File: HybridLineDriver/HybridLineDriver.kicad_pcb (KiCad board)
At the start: 2 copper layers, 100 x 50 mm, 60 parts, among them J1 XLR3, J2 Conn_01x03, J3 Conn_01x02, J4 XLR3, J5 Conn_01x02, U1 OPA1679, U2 OPA1679

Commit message: added comments
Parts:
- moved C14 9.23 mm to (114.3, 91.4)
- moved R24 5.43 mm to (109.2, 92.7), turned to -90 degrees
- moved C18 5.09 mm to (91.4, 91.4)
- moved J1 4.84 mm to (81.9, 85.7), turned to 90 degrees
- moved J4 4.26 mm to (101.0, 85.7), turned to 90 degrees
- moved R29 3.49 mm to (96.5, 93.2), turned to 90 degrees
- moved J3 2.62 mm to (80.0, 124.5), turned to -90 degrees
- moved R18 2.62 mm to (76.8, 88.9)
- moved J5 2.62 mm to (93.3, 124.5), turned to -90 degrees
- moved C6 2.29 mm to (72.4, 94.0)
- moved C2 1.77 mm to (80.0, 100.3)
- moved C5 1.42 mm to (72.4, 120.0)
- moved R6 1.34 mm to (83.0, 95.2)
- moved RV2 1.27 mm to (112.4, 123.9)
- moved R26 1.08 mm to (107.3, 123.9)
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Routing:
- net Net-(C18-Pad1): track 6.72 -> 17.7 mm
- net Net-(C14-Pad1): track 6.46 -> 16.6 mm
- net Net-(C6-Pad2): track 16.4 -> 26.1 mm
- net Net-(U2C-+): track 27.1 -> 30.4 mm
- net Net-(J5-Pin_1): track 14.1 -> 11.6 mm
- net Net-(J3-Pin_1): track 7.29 -> 9.46 mm
- net GND: track 32.0 -> 33.2 mm
- net Net-(C5-Pad2): track 19.2 -> 20.3 mm
- net Net-(U2D-+): track 26.0 -> 24.9 mm
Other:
- board text added: "GND"
- board text added: "IN"
- board text added: "IN+"
- board text added: "IN-"
- board text added: "OUT"
- board text added: "OUT+"
- board text added: "OUT-"
- board text added: "V+"
- board text added: "V-"

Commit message: updated comment layout
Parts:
- moved C5 0.64 mm to (71.8, 120.0)
- moved J1 0.64 mm to (81.3, 85.7)
- moved J5 0.64 mm to (94.0, 124.5)
- moved J3 0.63 mm to (80.6, 124.5)
- moved R6 0.44 mm to (82.5, 95.2)
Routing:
- net Net-(J3-Pin_1): track 9.46 -> 10.7 mm
- net Net-(J5-Pin_1): track 11.6 -> 10.8 mm
- net Net-(C6-Pad2): track 26.1 -> 25.4 mm
- net Net-(C5-Pad2): track 20.3 -> 19.7 mm
- net GND: track 33.2 -> 33.7 mm
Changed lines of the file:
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@@
 	(footprint "Connector_PinHeader_2.54mm:PinHeader_1x02_P2.54mm_Vertical"
 		(layer "F.Cu")
-		(at 80.01 124.46 -90)
+		(at 80.645 124.46 -90)
 		(descr "Through hole straight pin header, 1x02, 2.54mm pitch, single row")
 		(tags "Through hole pin header THT 1x02 2.54mm single row")
 		(property "Reference" "J3"
-			(at 0 -2.54 0)
+			(at 0 5.08 0)
 			(unlocked yes)
 			(layer "F.SilkS")
@@
 	(footprint "Resistor_SMD:R_1206_3216Metric"
 		(layer "F.Cu")
-		(at 82.9925 95.25)
+		(at 82.55 95.25)
 		(descr "Resistor SMD 1206 (3216 Metric), square (rectangular) end terminal, IPC_7351 nominal, (Body size source: IPC-SM-782 page 72, https://www.pcb-3d.com/wordpress/wp-content/uploads/ipc-sm-782a_amendment_1_and_2.pdf), generated with kicad-footprint-generator")
 		(tags "resistor")
@@
 		)
 		(property "Value" "100k"
-			(at 0 1.82 360)
+			(at 0 1.82 0)
 			(layer "F.Fab")
 			(effects
@@
 		)
 		(fp_text user "${REFERENCE}"
-			(at 0 0 360)
+			(at 0 0 0)
 			(layer "F.Fab")
 			(effects
@@
 		)
 		(property "Value" "10M"
-			(at 0 1.82 270)
+			(at 0 1.82 -90)
 			(layer "F.Fab")
 			(effects
@@
 		)
 		(fp_text user "${REFERENCE}"
-			(at 0 0 270)
+			(at 0 0 -90)
 			(layer "F.Fab")
 			(effects
@@
 	(footprint "Connector_PinHeader_2.54mm:PinHeader_1x03_P2.54mm_Vertical"
 		(layer "F.Cu")
-		(at 81.915 85.725 90)
+		(at 81.28 85.725 90)
 		(descr "Through hole straight pin header, 1x03, 2.54mm pitch, single row")
 		(tags "Through hole pin header THT 1x03 2.54mm single row")
 		(property "Reference" "J1"
-			(at 0 7.62 0)
+			(at 0 -2.54 0)
 			(unlocked yes)
 			(layer "F.SilkS")
@@
 		)
 		(property "Value" "XLR3"
-			(at 0 7.41 270)
+			(at 0 7.41 -90)
 			(layer "F.Fab")
 			(effects
@@
 		)
 		(fp_text user "${REFERENCE}"
-			(at 0 2.54 360)
+			(at 0 2.54 0)
 			(layer "F.Fab")
 			(effects
@@
 		(tags "Through hole pin header THT 1x03 2.54mm single row")
 		(property "Reference" "J4"
-			(at 0 7.62 0)
+			(at 0 -2.54 0)
 			(unlocked yes)
 			(layer "F.SilkS")
@@
 		)
 		(property "Value" "XLR3"
-			(at 0 7.41 270)
+			(at 0 7.41 -90)
 			(layer "F.Fab")
 			(effects
@@
 		)
 		(fp_text user "${REFERENCE}"
-			(at 0 2.54 360)
+			(at 0 2.54 0)
 			(layer "F.Fab")
 			(effects
@@
 	(footprint "Connector_PinHeader_2.54mm:PinHeader_1x02_P2.54mm_Vertical"
 		(layer "F.Cu")
-		(at 93.345 124.46 -90)
+		(at 93.98 124.46 -90)
 		(descr "Through hole straight pin header, 1x02, 2.54mm pitch, single row")
 		(tags "Through hole pin header THT 1x02 2.54mm single row")
 		(property "Reference" "J5"
-			(at 0 -2.54 0)
+			(at 0 5.08 0)
 			(unlocked yes)
 			(layer "F.SilkS")
@@
 		(tags "Through hole pin header THT 1x03 2.54mm single row")
 		(property "Reference" "J2"
-			(at -2.54 2.54 0)
+			(at 2.54 5.142 0)
 			(unlocked yes)
 			(layer "F.SilkS")
@@
 		(tags "resistor")
 		(property "Reference" "R27"
-			(at 0 -1.82 0)
+			(at 4.445 -0.062 0)
 			(unlocked yes)
 			(layer "F.SilkS")
@@
 	(footprint "Capacitor_THT:CP_Radial_D6.3mm_P2.50mm"
 		(layer "F.Cu")
-		(at 72.39 120.015 -90)
+		(at 71.755 120.015 -90)
 		(descr "CP, Radial series, Radial, pin pitch=2.50mm, , diameter=6.3mm, Electrolytic Capacitor")
 		(tags "CP Radial series Radial pin pitch 2.50mm  diameter 6.3mm Electrolytic Capacitor")
@@
 	)
 	(gr_text "IN"
-		(at 80.645 130.175 90)
+		(at 81.28 130.175 90)
 		(layer "Cmts.User")
 		(effects
@@
 	)
 	(gr_text "OUT"
-		(at 93.98 130.175 90)
+		(at 94.615 130.175 90)
 		(layer "Cmts.User")
 		(effects
@@
 	)
 	(gr_text "GND"
-		(at 82.55 92.71 90)
+		(at 81.915 92.71 90)
 		(layer "Cmts.User")
 		(effects
@@
 	)
 	(gr_text "OUT+"
-		(at 87.63 92.71 90)
+		(at 86.995 92.71 90)
 		(layer "Cmts.User")
 		(effects
@@
 	)
 	(gr_text "GND"
-		(at 91.44 130.175 90)
+		(at 92.075 130.175 90)
 		(layer "Cmts.User")
 		(effects
@@
 	)
 	(gr_text "OUT-"
-		(at 85.09 92.71 90)
+		(at 84.455 92.71 90)
 		(layer "Cmts.User")
 		(effects
@@
 	)
 	(gr_text "GND"
-		(at 78.105 130.175 90)
+		(at 78.74 130.175 90)
 		(layer "Cmts.User")
 		(effects
@@
 	)
 	(segment
+		(start 83.82 85.725)
+		(end 83.82 95.0575)
+		(width 0.254)
+		(layer "F.Cu")
+		(net 4)
+	)
+	(segment
 		(start 80.01 103.83)
 		(end 80.32 103.83)
@@
 	)
 	(segment
-		(start 84.455 85.725)
-		(end 84.455 95.25)
+		(start 84.0125 99.8275)
+		(end 84.0125 95.25)
 		(width 0.254)
 		(layer "F.Cu")
@@
 	)
 	(segment
-		(start 84.455 99.385)
-		(end 84.455 95.25)
+		(start 80.01 103.83)
+		(end 84.0125 99.8275)
 		(width 0.254)
 		(layer "F.Cu")
@@
 	)
 	(segment
-		(start 80.01 103.83)
-		(end 84.455 99.385)
+		(start 83.82 95.0575)
+		(end 84.0125 95.25)
 		(width 0.254)
 		(layer "F.Cu")
@@
 	)
 	(segment
-		(start 52.959 124.6525)
-		(end 53.1515 124.46)
+		(start 69.81 124.46)
+		(end 71.755 122.515)
 		(width 0.25)
 		(layer "F.Cu")
@@
 	)
 	(segment
-		(start 70.445 124.46)
-		(end 72.39 122.515)
+		(start 53.1515 124.46)
+		(end 69.81 124.46)
 		(width 0.25)
 		(layer "F.Cu")
@@
 	)
 	(segment
-		(start 53.1515 124.46)
-		(end 70.445 124.46)
+		(start 52.959 124.6525)
+		(end 53.1515 124.46)
 		(width 0.25)
 		(layer "F.Cu")
@@
 	(segment
 		(start 75.565 120.015)
-		(end 72.39 120.015)
+		(end 71.755 120.015)
+		(width 0.254)
+		(layer "F.Cu")
+		(net 10)
+	)
+	(segment
+		(start 80.645 124.46)
+		(end 80.01 124.46)
 		(width 0.254)
 		(layer "F.Cu")
@@
 	)
 	(segment
-		(start 77.47 83.82)
-		(end 85.09 83.82)
+		(start 72.39 97.48)
+		(end 72.39 97.155)
 		(width 0.254)
 		(layer "F.Cu")
@@
 	)
 	(segment
-		(start 85.09 83.82)
-		(end 86.995 85.725)
+		(start 75.3725 88.9)
+		(end 75.3725 85.9175)
 		(width 0.254)
 		(layer "F.Cu")
@@
 	)
 	(segment
-		(start 72.39 97.48)
-		(end 72.39 97.155)
+		(start 84.455 83.82)
+		(end 86.36 85.725)
 		(width 0.254)
 		(layer "F.Cu")
@@
 	)
 	(segment
-		(start 75.3725 85.9175)
-		(end 77.47 83.82)
+		(start 75.3725 94.1725)
+		(end 75.3725 88.9)
 		(width 0.254)
 		(layer "F.Cu")
@@
 	)
 	(segment
-		(start 75.3725 94.1725)
-		(end 75.3725 88.9)
+		(start 77.47 83.82)
+		(end 84.455 83.82)
 		(width 0.254)
 		(layer "F.Cu")
@@
 	)
 	(segment
-		(start 75.3725 88.9)
-		(end 75.3725 85.9175)
+		(start 75.3725 85.9175)
+		(end 77.47 83.82)
 		(width 0.254)
 		(layer "F.Cu")
@@
 	)
 	(segment
-		(start 79.375 90.805)
-		(end 78.2975 89.7275)
-		(width 0.254)
-		(layer "F.Cu")
-		(net 15)
-	)
-	(segment
 		(start 56.72 121.49)
 		(end 56.515 121.285)
@@
 	)
 	(segment
+		(start 78.2975 90.9975)
+		(end 78.2975 88.9)
+		(width 0.254)
+		(layer "F.Cu")
+		(net 15)
+	)
+	(segment
+		(start 81.0875 95.25)
+		(end 79.375 95.25)
+		(width 0.254)
+		(layer "F.Cu")
+		(net 15)
+	)
+	(segment
 		(start 103.6975 115.567)
 		(end 103.6975 116.267)
@@
 	)
 	(segment
-		(start 81.53 95.25)
-		(end 80.01 95.25)
-		(width 0.254)
-		(layer "F.Cu")
-		(net 15)
-	)
-	(segment
 		(start 98.81 91.69)
 		(end 99.06 91.44)
@@
 	)
 	(segment
-		(start 78.2975 89.7275)
-		(end 78.2975 88.9)
+		(start 78.74 91.44)
+		(end 78.2975 90.9975)
 		(width 0.254)
 		(layer "F.Cu")
@@
 	)
 	(via
-		(at 80.01 95.25)
+		(at 79.375 95.25)
 		(size 0.8)
 		(drill 0.4)
@@
 	)
 	(via
-		(at 79.375 90.805)
+		(at 78.74 91.44)
 		(size 0.8)
 		(drill 0.4)
@@
 	)
 	(segment
-		(start 93.345 124.46)
-		(end 92.71 124.46)
+		(start 93.98 124.46)
+		(end 88.9 119.38)
 		(width 0.254)
 		(layer "F.Cu")
@@
 	)
 	(segment
-		(start 88.9 120.65)
+		(start 88.9 119.38)
 		(end 88.9 119.34)
 		(width 0.254)
@@
 	)
 	(segment
-		(start 93.345 124.46)
+		(start 93.98 124.46)
 		(end 97.5975 124.46)
 		(width 0.254)
 		(layer "F.Cu")
-		(net 26)
-	)
-	(segment
-		(start 92.71 124.46)
-		(end 88.9 120.65)
-		(width 0.254)
-		(layer "F.Cu")

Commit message: update traces
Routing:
- net Net-(R2-Pad1): track 21.9 -> 18.3 mm
- net Net-(U2A--): track 30.1 -> 32.3 mm
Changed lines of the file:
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@@
+	)
+	(segment
+		(start 72.39 107.1265)
+		(end 72.644 106.8725)
+		(width 0.254)
+		(layer "F.Cu")
+		(net 16)
 	)
 	(segment
@@
 	)
 	(segment
-		(start 72.8365 115.3775)
-		(end 75.184 113.03)
-		(width 0.254)
-		(layer "F.Cu")
-		(net 16)
-	)
-	(segment
 		(start 72.8365 106.8725)
 		(end 72.644 106.8725)
@@
 	(segment
 		(start 67.564 115.3775)
-		(end 72.8365 115.3775)
-		(width 0.254)
-		(layer "F.Cu")
-		(net 16)
-	)
-	(segment
-		(start 75.184 109.4125)
-		(end 72.644 106.8725)
+		(end 67.7565 115.57)
 		(width 0.254)
 		(layer "F.Cu")
@@
 	)
 	(segment
-		(start 75.184 113.03)
-		(end 75.184 109.4125)
+		(start 67.7565 115.57)
+		(end 69.75375 115.57)
+		(width 0.254)
+		(layer "F.Cu")
+		(net 16)
+	)
+	(segment
+		(start 72.39 112.93375)
+		(end 72.39 107.1265)
+		(width 0.254)
+		(layer "F.Cu")
+		(net 16)
+	)
+	(segment
+		(start 69.75375 115.57)
+		(end 72.39 112.93375)
 		(width 0.254)
 		(layer "F.Cu")
@@
 	)
 	(segment
+		(start 107.6925 110.617)
+		(end 106.2375 110.617)
+		(width 0.254)
+		(layer "F.Cu")
+		(net 24)
+	)
+	(segment
 		(start 106.2375 102.7395)
 		(end 106.2375 110.617)
@@
 	)
 	(segment
-		(start 107.6925 110.617)
-		(end 106.2375 110.617)
-		(width 0.254)
-		(layer "F.Cu")
-		(net 24)
-	)
-	(segment
 		(start 111.76 104.0095)
 		(end 109.6625 106.107)
@@
 	)
 	(segment
+		(start 93.1525 108.647)
+		(end 93.1525 108.7775)
+		(width 0.254)
+		(layer "F.Cu")
+		(net 35)
+	)
+	(segment
+		(start 90.17 118.11)
+		(end 92.28 120.22)
+		(width 0.254)
+		(layer "F.Cu")
+		(net 35)
+	)
+	(segment
+		(start 93.1525 108.647)
+		(end 88.838 108.647)
+		(width 0.254)
+		(layer "F.Cu")
+		(net 35)
+	)
+	(segment
+		(start 98.0445 120.2075)
+		(end 99.8875 118.3645)
+		(width 0.254)
+		(layer "F.Cu")
+		(net 35)
+	)
+	(segment
+		(start 99.8875 118.3645)
+		(end 99.8875 115.567)
+		(width 0.254)
+		(layer "F.Cu")
+		(net 35)
+	)
+	(segment
+		(start 86.995 117.475)
+		(end 87.63 118.11)
+		(width 0.254)
+		(layer "F.Cu")
+		(net 35)
+	)
+	(segment
+		(start 93.98 120.22)
+		(end 96.5075 120.22)
+		(width 0.254)
+		(layer "F.Cu")
+		(net 35)
+	)
+	(segment
 		(start 92.28 120.22)
 		(end 93.98 120.22)
@@
 	)
 	(segment
-		(start 93.1525 108.647)
-		(end 93.1525 108.7775)
-		(width 0.254)
-		(layer "F.Cu")
-		(net 35)
-	)
-	(segment
-		(start 92.58275 108.647)
-		(end 86.995 114.23475)
-		(width 0.254)
-		(layer "F.Cu")
-		(net 35)
-	)
-	(segment
-		(start 98.0445 120.2075)
-		(end 99.8875 118.3645)
-		(width 0.254)
-		(layer "F.Cu")
-		(net 35)
-	)
-	(segment
-		(start 99.8875 118.3645)
+		(start 96.5075 120.22)
+		(end 96.52 120.2075)
+		(width 0.254)
+		(layer "F.Cu")
+		(net 35)
+	)
+	(segment
+		(start 86.995 110.49)
+		(end 86.995 117.475)
+		(width 0.254)
+		(layer "F.Cu")
+		(net 35)
+	)
+	(segment
+		(start 96.52 120.2075)
+		(end 98.0445 120.2075)
+		(width 0.254)
+		(layer "F.Cu")
+		(net 35)
+	)
+	(segment
+		(start 99.8875 115.183264)
 		(end 99.8875 115.567)
 		(width 0.254)
@@
 	)
 	(segment
-		(start 90.17 118.11)
-		(end 92.28 120.22)
-		(width 0.254)
-		(layer "F.Cu")
-		(net 35)
-	)
-	(segment
-		(start 86.995 114.23475)
-		(end 86.995 117.475)
-		(width 0.254)
-		(layer "F.Cu")
-		(net 35)
-	)
-	(segment
-		(start 93.98 120.22)
-		(end 96.5075 120.22)
+		(start 88.838 108.647)
+		(end 86.995 110.49)
+		(width 0.254)
+		(layer "F.Cu")
+		(net 35)
+	)
+	(segment
+		(start 99.695 115.7595)
+		(end 99.8875 115.567)
 		(width 0.254)
 		(layer "F.Cu")
@@
 	)
 	(segment
-		(start 96.5075 120.22)
-		(end 96.52 120.2075)
-		(width 0.254)
-		(layer "F.Cu")
-		(net 35)
-	)
-	(segment
-		(start 86.995 117.475)
-		(end 87.63 118.11)
-		(width 0.254)
-		(layer "F.Cu")
-		(net 35)
-	)
-	(segment
-		(start 96.52 120.2075)
-		(end 98.0445 120.2075)
-		(width 0.254)
-		(layer "F.Cu")
-		(net 35)
-	)
-	(segment
-		(start 99.8875 115.183264)
-		(end 99.8875 115.567)
-		(width 0.254)
-		(layer "F.Cu")
-		(net 35)
-	)
-	(segment
-		(start 93.1525 108.647)
-		(end 92.58275 108.647)
-		(width 0.254)
-		(layer "F.Cu")
-		(net 35)
-	)
-	(segment
-		(start 99.695 115.7595)
-		(end 99.8875 115.567)
-		(width 0.254)
-		(layer "F.Cu")
-		(net 35)
-	)
-	(segment
 		(start 101.6 120.077)
 		(end 100.965 119.442)
@@
 	)
 	(segment
+		(start 100.965 119.442)
+		(end 100.965 115.7595)
+		(width 0.254)
+		(layer "F.Cu")
+		(net 36)
+	)
+	(segment
+		(start 107.745 118.172)
+		(end 105.84 120.077)
+		(width 0.254)
+		(layer "F.Cu")
+		(net 36)
+	)
+	(segment
+		(start 105.8525 123.887)
+		(end 105.84 123.8745)
+		(width 0.254)
+		(layer "F.Cu")
+		(net 36)
+	)
+	(segment
 		(start 109.855 118.172)
 		(end 107.745 118.172)
@@
 	)
 	(segment
+		(start 111.125 110.1095)
+		(end 111.125 116.902)
+		(width 0.254)
+		(layer "F.Cu")
+		(net 36)
+	)
+	(segment
+		(start 100.965 115.7595)
+		(end 101.1575 115.567)
+		(width 0.254)
+		(layer "F.Cu")
+		(net 36)
+	)
+	(segment
+		(start 105.84 120.077)
+		(end 101.6 120.077)
+		(width 0.254)
+		(layer "F.Cu")
+		(net 36)
+	)
+	(segment
 		(start 111.125 116.902)
 		(end 109.855 118.172)
@@
 	)
 	(segment
+		(start 105.84 123.8745)
+		(end 105.84 120.077)
+		(width 0.254)
+		(layer "F.Cu")
+		(net 36)
+	)
+	(segment
 		(start 111.3175 109.917)
 		(end 111.125 110.1095)
-		(width 0.254)
-		(layer "F.Cu")
-		(net 36)
-	)
-	(segment
-		(start 100.965 119.442)
-		(end 100.965 115.7595)
-		(width 0.254)
-		(layer "F.Cu")
-		(net 36)
-	)
-	(segment
-		(start 111.125 110.1095)
-		(end 111.125 116.902)
-		(width 0.254)
-		(layer "F.Cu")
-		(net 36)
-	)
-	(segment
-		(start 105.8525 123.887)
-		(end 105.84 123.8745)
-		(width 0.254)
-		(layer "F.Cu")
-		(net 36)
-	)
-	(segment
-		(start 107.745 118.172)
-		(end 105.84 120.077)
-		(width 0.254)
-		(layer "F.Cu")
-		(net 36)
-	)
-	(segment
-		(start 100.965 115.7595)
-		(end 101.1575 115.567)
-		(width 0.254)
-		(layer "F.Cu")
-		(net 36)
-	)
-	(segment
-		(start 105.84 120.077)
-		(end 101.6 120.077)
-		(width 0.254)
-		(layer "F.Cu")
-		(net 36)
-	)
-	(segment
-		(start 105.84 123.8745)
-		(end 105.84 120.077)
 		(width 0.254)
 		(layer "F.Cu")
@@
 		(polygon
 			(pts
-				(xy 95.123 109.728) (xy 64.008 109.728) (xy 64.008 116.713) (xy 95.123 116.713)
+				(xy 95.123 109.728) (xy 66.675 109.728) (xy 66.675 116.713) (xy 95.123 116.713)
 			)
 		)
@@
 		(polygon
 			(pts
-				(xy 132.588 109.855) (xy 107.823 109.855) (xy 107.823 116.84) (xy 132.588 116.84)
+				(xy 132.08 109.855) (xy 107.95 109.855) (xy 107.95 116.84) (xy 132.08 116.84)
 			)
 		)

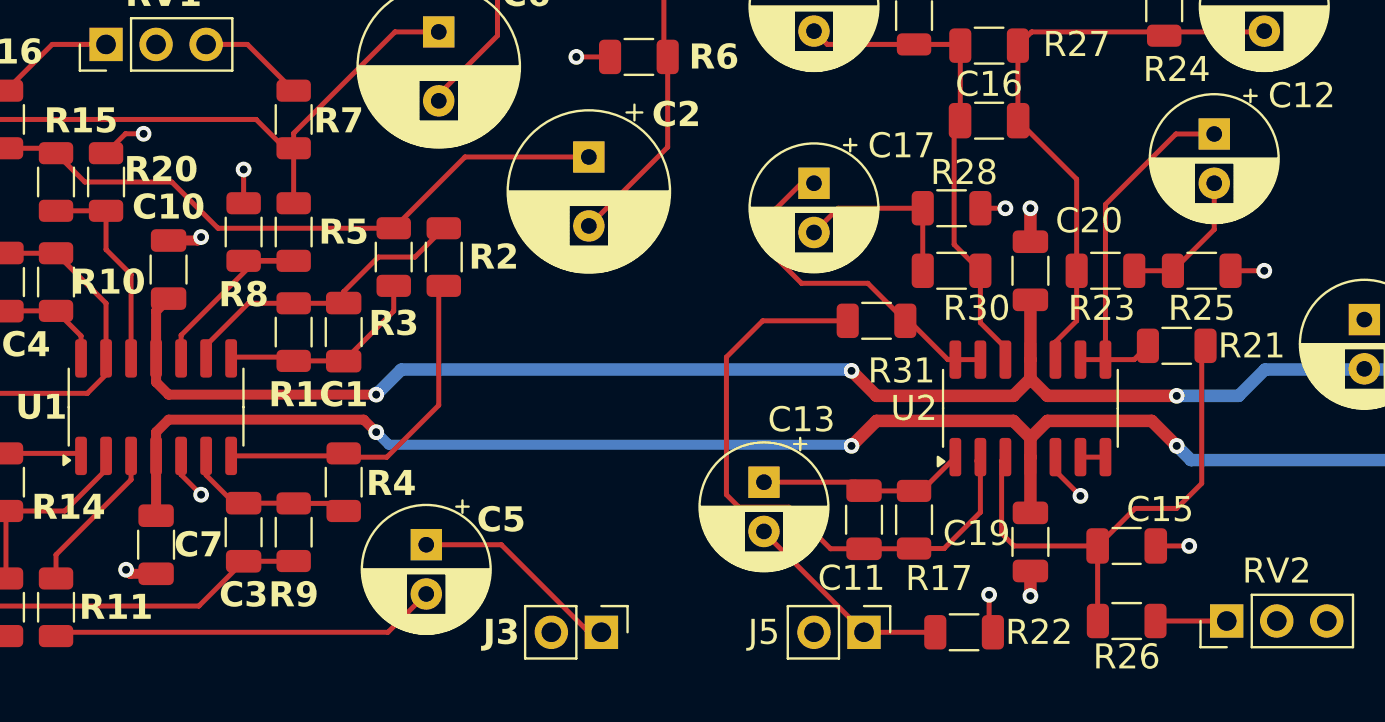
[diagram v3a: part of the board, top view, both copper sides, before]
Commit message: added more vias
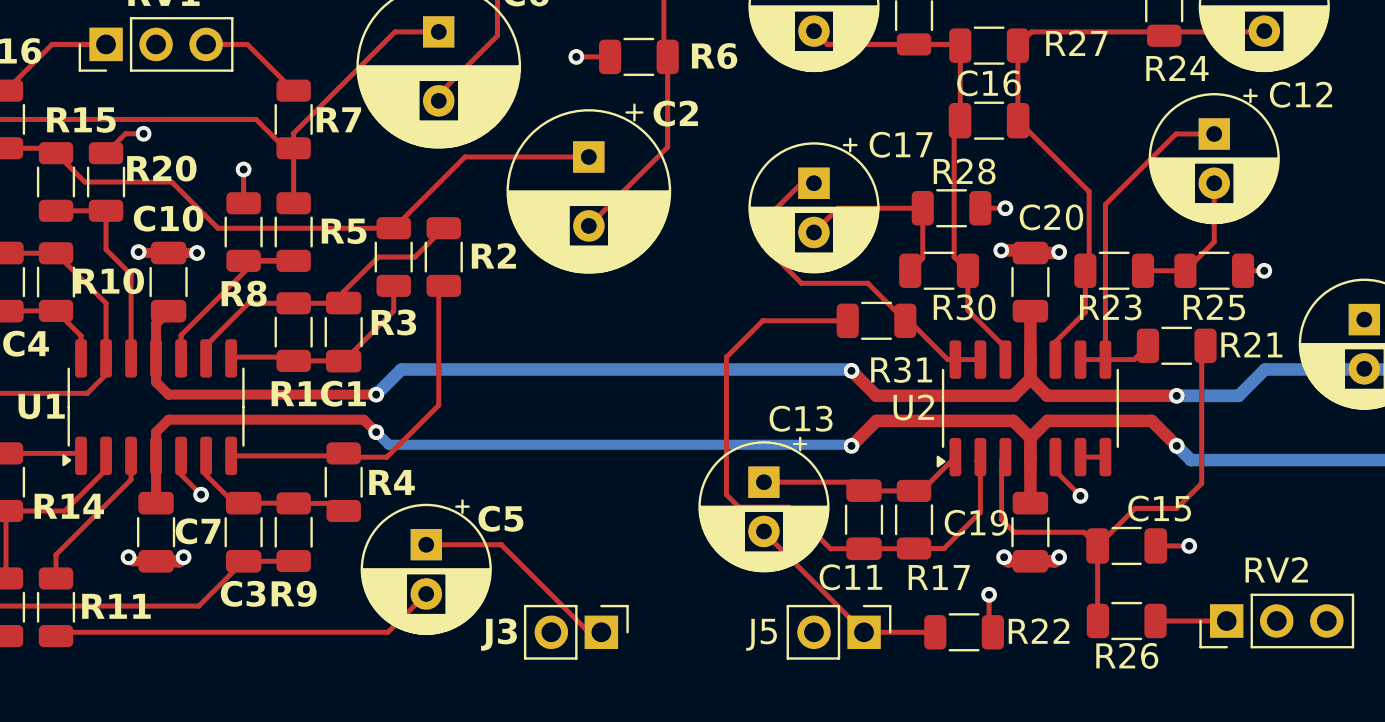
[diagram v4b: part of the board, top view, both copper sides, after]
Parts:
- moved C10 0.64 mm to (58.7, 106.7)
- moved C7 0.64 mm to (58.0, 119.4)
- moved R25 0.64 mm to (111.8, 106.1)
- moved R30 0.63 mm to (97.8, 106.1)
- moved C20 0.57 mm to (102.4, 106.7)
- moved C19 0.49 mm to (102.4, 119.4)
- moved R23 0.44 mm to (106.7, 106.1)
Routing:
- net GND: track 33.7 -> 38.4 mm, vias 17 -> 21
- net -15V: track 83.9 -> 82.7 mm
- net +15V: track 84.5 -> 83.4 mm
- net Net-(U2C-+): track 30.4 -> 31.0 mm

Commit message: PCB now has an Uterus
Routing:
- net GND: track 38.4 -> 41.8 mm
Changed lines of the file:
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@@
+	)
+	(segment
+		(start 102.362 121.666)
+		(end 101.473 120.777)
+		(width 0.635)
+		(layer "F.Cu")
+		(net 15)
+	)
+	(segment
+		(start 100.98125 120.777)
+		(end 102.47275 120.777)
+		(width 0.635)
+		(layer "F.Cu")
+		(net 15)
 	)
 	(segment
@@
 	)
 	(segment
+		(start 103.85325 120.777)
+		(end 102.90275 120.777)
+		(width 0.635)
+		(layer "F.Cu")
+		(net 15)
+	)
+	(segment
 		(start 108.79 120.077)
 		(end 110.49 120.077)
@@
 	)
 	(segment
-		(start 101.297 120.855)
-		(end 102.4275 120.855)
-		(width 0.635)
-		(layer "F.Cu")
-		(net 15)
-	)
-	(segment
 		(start 57.15 105.156)
 		(end 57.404 105.156)
@@
 	)
 	(segment
-		(start 103.886 120.65)
-		(end 103.681 120.855)
-		(width 0.635)
-		(layer "F.Cu")
-		(net 15)
-	)
-	(segment
 		(start 59.231 120.855)
 		(end 58.039 120.855)
@@
 	)
 	(segment
+		(start 102.362 121.793)
+		(end 103.378 120.777)
+		(width 0.635)
+		(layer "F.Cu")
+		(net 15)
+	)
+	(segment
 		(start 103.6975 115.567)
 		(end 103.6975 116.267)
@@
 	)
 	(segment
+		(start 100.936 120.855)
+		(end 100.633 121.158)
+		(width 0.635)
+		(layer "F.Cu")
+		(net 15)
+	)
+	(segment
 		(start 102.294947 105.072447)
 		(end 102.4275 105.205)
@@
 	)
 	(segment
+		(start 104.189 121.158)
+		(end 103.886 120.855)
+		(width 0.635)
+		(layer "F.Cu")
+		(net 15)
+	)
+	(segment
+		(start 102.362 122.174)
+		(end 102.362 121.793)
+		(width 0.635)
+		(layer "F.Cu")
+		(net 15)
+	)
+	(segment
 		(start 98.81 91.69)
 		(end 99.06 91.44)
@@
 	)
 	(segment
-		(start 103.681 120.855)
-		(end 102.4275 120.855)
-		(width 0.635)
-		(layer "F.Cu")
-		(net 15)
-	)
-	(segment
-		(start 101.092 120.65)
-		(end 101.297 120.855)
-		(width 0.635)
-		(layer "F.Cu")
-		(net 15)
-	)
-	(segment
 		(start 59.309 116.459)
 		(end 59.309 115.505)
@@
 	)
 	(via
-		(at 101.092 120.65)
+		(at 100.633 121.158)
 		(size 0.8)
 		(drill 0.4)
@@
 	)
 	(via
-		(at 103.886 120.65)
-		(size 0.8)
-		(drill 0.4)
+		(at 104.189 121.158)
+		(size 0.8)
+		(drill 0.4)
